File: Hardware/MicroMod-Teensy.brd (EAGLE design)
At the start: 22 x 22.8 mm, 82 parts, among them J1 MICROMOD-2222, Q1 20V/4.2A/52mΩ/1.4W, Q2 20V/0.2A/8MHz/1.2Ω/1Vth, U1 IMXRT1062DV10X10, U3 MKL02Z32VFG4, U4 W25QXX128MBIT-6X5, Y1 32.768kHz, Y2 24MHz

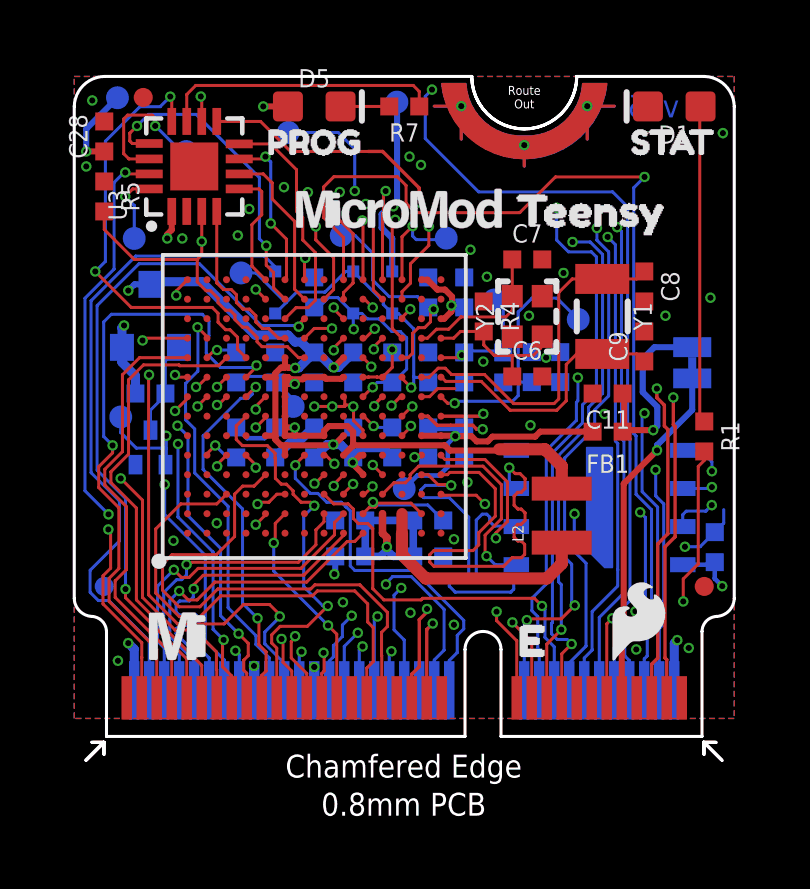
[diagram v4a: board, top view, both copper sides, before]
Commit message: Adding production panel files
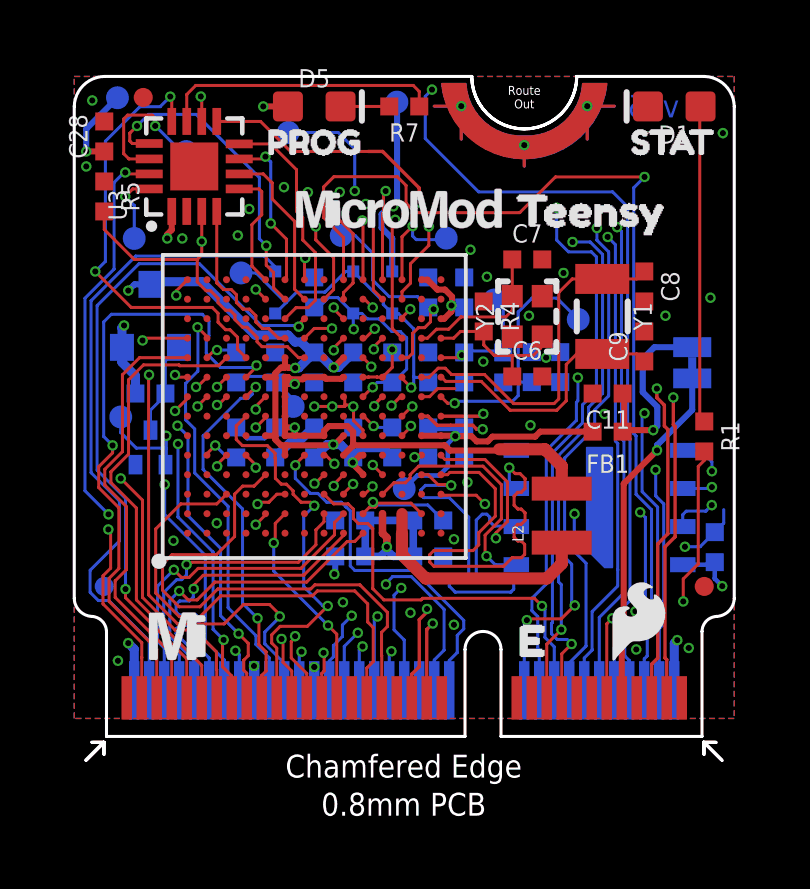
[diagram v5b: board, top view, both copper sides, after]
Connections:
- net SWD_CLK: no longer J1.21
- net SWD_DIO: no longer J1.23
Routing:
- net SWD_DIO: track 36.2 -> 2.43 mm, vias 3 -> 1
- net SWD_CLK: track 37.0 -> 4.89 mm, vias 3 -> 1
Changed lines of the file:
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@@
 <?xml version="1.0" encoding="utf-8"?>
 <!DOCTYPE eagle SYSTEM "eagle.dtd">
-<eagle version="9.6.0">
+<eagle version="9.5.2">
 <drawing>
 <settings>
@@
 <setting verticaltext="up"/>
 </settings>
-<grid distance="1" unitdist="mm" unit="mm" style="lines" multiple="1" display="yes" altdistance="0.1" altunitdist="mm" altunit="mm"/>
+<grid distance="0.05" unitdist="inch" unit="inch" style="lines" multiple="1" display="yes" altdistance="0.005" altunitdist="inch" altunit="inch"/>
 <layers>
-<layer number="1" name="Top" color="4" fill="1" visible="yes" active="yes"/>
-<layer number="2" name="Vert-GND" color="1" fill="3" visible="no" active="yes"/>
+<layer number="1" name="Top" color="4" fill="1" visible="no" active="yes"/>
+<layer number="2" name="Vert-GND" color="1" fill="3" visible="yes" active="yes"/>
 <layer number="15" name="Horz-3V3" color="4" fill="6" visible="no" active="yes"/>
-<layer number="16" name="Bottom" color="1" fill="1" visible="yes" active="yes"/>
+<layer number="16" name="Bottom" color="1" fill="1" visible="no" active="yes"/>
 <layer number="17" name="Pads" color="2" fill="1" visible="yes" active="yes"/>
 <layer number="18" name="Vias" color="2" fill="1" visible="yes" active="yes"/>
 <layer number="19" name="Unrouted" color="6" fill="1" visible="yes" active="yes"/>
 <layer number="20" name="Dimension" color="24" fill="1" visible="yes" active="yes"/>
-<layer number="21" name="tPlace" color="16" fill="1" visible="yes" active="yes"/>
-<layer number="22" name="bPlace" color="14" fill="1" visible="yes" active="yes"/>
-<layer number="23" name="tOrigins" color="15" fill="1" visible="yes" active="yes"/>
-<layer number="24" name="bOrigins" color="15" fill="1" visible="yes" active="yes"/>
+<layer number="21" name="tPlace" color="16" fill="1" visible="no" active="yes"/>
+<layer number="22" name="bPlace" color="14" fill="1" visible="no" active="yes"/>
+<layer number="23" name="tOrigins" color="15" fill="1" visible="no" active="yes"/>
+<layer number="24" name="bOrigins" color="15" fill="1" visible="no" active="yes"/>
 <layer number="25" name="tNames" color="7" fill="1" visible="no" active="yes"/>
 <layer number="26" name="bNames" color="7" fill="1" visible="no" active="yes"/>
@@
 <layer number="43" name="vRestrict" color="2" fill="10" visible="no" active="yes"/>
 <layer number="44" name="Drills" color="7" fill="1" visible="no" active="yes"/>
-<layer number="45" name="Holes" color="7" fill="1" visible="yes" active="yes"/>
+<layer number="45" name="Holes" color="7" fill="1" visible="no" active="yes"/>
 <layer number="46" name="Milling" color="3" fill="1" visible="no" active="yes"/>
 <layer number="47" name="Measures" color="7" fill="1" visible="no" active="yes"/>
 <layer number="48" name="Document" color="7" fill="1" visible="no" active="yes"/>
-<layer number="49" name="Reference" color="7" fill="1" visible="yes" active="yes"/>
+<layer number="49" name="Reference" color="7" fill="1" visible="no" active="yes"/>
 <layer number="50" name="dxf" color="7" fill="1" visible="no" active="yes"/>
-<layer number="51" name="tDocu" color="6" fill="1" visible="yes" active="yes"/>
+<layer number="51" name="tDocu" color="6" fill="1" visible="no" active="yes"/>
 <layer number="52" name="bDocu" color="7" fill="1" visible="no" active="yes"/>
 <layer number="91" name="Nets" color="2" fill="1" visible="no" active="no"/>
@@
 <wire x1="3.561" y1="19.487" x2="2.7" y2="20.348" width="0.1016" layer="16"/>
 <wire x1="2.7" y1="20.348" x2="2.7" y2="20.34" width="0.1016" layer="16"/>
-<via x="14.605" y="3.7913" extent="1-16" drill="0.2"/>
-<via x="11.176" y="19.31865" extent="1-16" drill="0.2"/>
-<wire x1="14.605" y1="3.7877125" x2="14.605" y2="3.7913" width="0.1016" layer="1"/>
-<wire x1="15.25" y1="3.1427125" x2="14.605" y2="3.7877125" width="0.1016" layer="1"/>
-<wire x1="15.25" y1="1.275" x2="15.25" y2="3.1427125" width="0.1016" layer="1"/>
-<wire x1="11.176" y1="19.31865" x2="10.5141" y2="19.98055" width="0.1016" layer="15"/>
-<wire x1="2.7" y1="20.34" x2="3.05945" y2="19.98055" width="0.1016" layer="15"/>
-<wire x1="10.5141" y1="19.98055" x2="3.05945" y2="19.98055" width="0.1016" layer="15"/>
-<wire x1="14.605" y1="3.7913" x2="14.605" y2="4.05461875" width="0.1143" layer="2"/>
-<wire x1="14.605" y1="4.05461875" x2="17.31485" y2="6.76446875" width="0.1143" layer="2"/>
-<wire x1="13.23074375" y1="19.37495" x2="11.2323" y2="19.37495" width="0.1143" layer="2"/>
-<wire x1="17.31485" y1="15.29084375" x2="13.23074375" y2="19.37495" width="0.1143" layer="2"/>
-<contactref element="J1" pad="21"/>
-<wire x1="11.2323" y1="19.37495" x2="11.176" y2="19.31865" width="0.1143" layer="2"/>
-<wire x1="17.31485" y1="6.76446875" x2="17.319" y2="6.76861875" width="0.1016" layer="2"/>
-<wire x1="17.319" y1="15.28669375" x2="17.31485" y2="15.29084375" width="0.1016" layer="2"/>
-<wire x1="17.319" y1="6.76861875" x2="17.319" y2="15.28669375" width="0.1016" layer="2"/>
 <wire x1="1.6468" y1="19.4162" x2="1.6468" y2="20.5698" width="0.1016" layer="1"/>
 <wire x1="1.6468" y1="20.5698" x2="1.778" y2="20.701" width="0.1016" layer="1"/>
@@
 <wire x1="1.7" y1="17.99" x2="2" y2="17.69" width="0.1016" layer="16"/>
 <wire x1="2" y1="17.69" x2="2" y2="16.59" width="0.1016" layer="16"/>
-<via x="14.078" y="4.15" extent="1-16" drill="0.2"/>
-<via x="11.557" y="19.04" extent="1-16" drill="0.2"/>
-<wire x1="14.75" y1="3.178" x2="14.078" y2="3.85" width="0.1016" layer="1"/>
-<wire x1="14.078" y1="3.85" x2="14.078" y2="4.15" width="0.1016" layer="1"/>
-<wire x1="14.75" y1="3.178" x2="14.75" y2="1.275" width="0.1016" layer="1"/>
-<wire x1="14.078" y1="4.15" x2="14.39505" y2="4.15" width="0.1143" layer="2"/>
-<wire x1="14.39505" y1="4.15" x2="17.09895" y2="6.8539" width="0.1143" layer="2"/>
-<wire x1="17.09895" y1="15.13305" x2="13.192" y2="19.04" width="0.1143" layer="2"/>
-<wire x1="13.192" y1="19.04" x2="11.557" y2="19.04" width="0.1143" layer="2"/>
-<contactref element="J1" pad="23"/>
-<wire x1="17.09895" y1="6.8539" x2="17.1158" y2="6.87075" width="0.1016" layer="2"/>
-<wire x1="17.1158" y1="15.1162" x2="17.09895" y2="15.13305" width="0.1016" layer="2"/>
-<wire x1="17.1158" y1="6.87075" x2="17.1158" y2="15.1162" width="0.1016" layer="2"/>
-<wire x1="11.557" y1="19.04" x2="11.3620625" y2="19.04" width="0.1016" layer="15"/>
-<wire x1="11.3620625" y1="19.04" x2="11.3121125" y2="18.99005" width="0.1016" layer="15"/>
-<wire x1="11.3121125" y1="18.99005" x2="11.0398875" y2="18.99005" width="0.1016" layer="15"/>
-<wire x1="11.0398875" y1="18.99005" x2="10.8474" y2="19.1825375" width="0.1016" layer="15"/>
-<wire x1="10.8474" y1="19.1825375" x2="10.8474" y2="19.35988125" width="0.1016" layer="15"/>
-<wire x1="10.8474" y1="19.35988125" x2="10.42993125" y2="19.77735" width="0.1016" layer="15"/>
-<wire x1="10.42993125" y1="19.77735" x2="3.48735" y2="19.77735" width="0.1016" layer="15"/>
-<wire x1="3.48735" y1="19.77735" x2="1.7" y2="17.99" width="0.1016" layer="15"/>
 </signal>
 <signal name="USB_D-" class="1">

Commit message: Move trace away from top edge
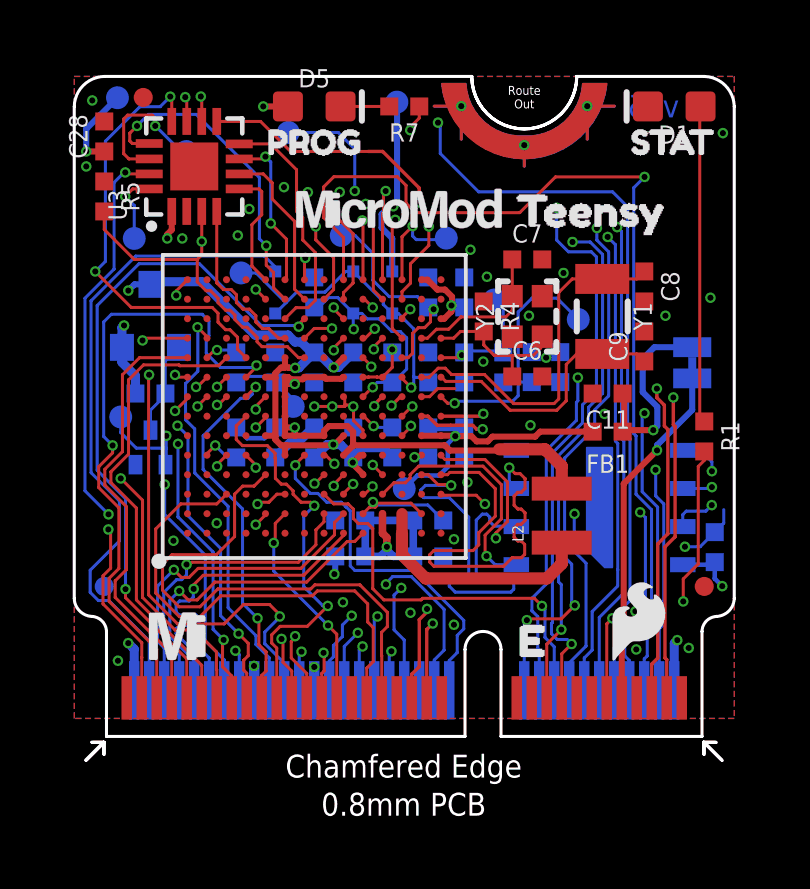
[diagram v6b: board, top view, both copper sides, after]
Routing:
- net PROGRAM: track 34.8 -> 33.9 mm
- net N$12: track 9.36 -> 9.70 mm, vias 0 -> 2
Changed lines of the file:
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@@
 <setting verticaltext="up"/>
 </settings>
-<grid distance="0.05" unitdist="inch" unit="inch" style="lines" multiple="1" display="yes" altdistance="0.005" altunitdist="inch" altunit="inch"/>
+<grid distance="1" unitdist="mm" unit="mm" style="lines" multiple="1" display="yes" altdistance="0.1" altunitdist="mm" altunit="mm"/>
 <layers>
 <layer number="1" name="Top" color="4" fill="1" visible="no" active="yes"/>
-<layer number="2" name="Vert-GND" color="1" fill="3" visible="yes" active="yes"/>
-<layer number="15" name="Horz-3V3" color="4" fill="6" visible="no" active="yes"/>
+<layer number="2" name="Vert-GND" color="1" fill="3" visible="no" active="yes"/>
+<layer number="15" name="Horz-3V3" color="4" fill="6" visible="yes" active="yes"/>
 <layer number="16" name="Bottom" color="1" fill="1" visible="no" active="yes"/>
 <layer number="17" name="Pads" color="2" fill="1" visible="yes" active="yes"/>
@@
 <wire x1="18.5238" y1="9.92411875" x2="18.4452" y2="10.00271875" width="0.1016" layer="16"/>
 <wire x1="13.48" y1="18.143" x2="17.945" y2="18.143" width="0.1016" layer="16"/>
-<wire x1="4.2188875" y1="21.3211125" x2="11.6961125" y2="21.3211125" width="0.1016" layer="15"/>
-<wire x1="11.6961125" y1="21.3211125" x2="11.925" y2="21.55" width="0.1016" layer="15"/>
-<via x="11.925" y="21.55" extent="1-16" drill="0.2"/>
-<wire x1="11.925" y1="21.55" x2="11.7" y2="21.325" width="0.1016" layer="16"/>
-<wire x1="11.7" y1="21.325" x2="11.7" y2="19.923" width="0.1016" layer="16"/>
-<wire x1="11.7" y1="19.923" x2="13.48" y2="18.143" width="0.1016" layer="16"/>
+<wire x1="4.2188875" y1="21.3211125" x2="11.2538875" y2="21.3211125" width="0.1016" layer="15"/>
+<wire x1="11.2538875" y1="21.3211125" x2="12.125" y2="20.45" width="0.1016" layer="15"/>
+<via x="12.125" y="20.45" extent="1-16" drill="0.2"/>
+<wire x1="12.125" y1="20.45" x2="12.2" y2="20.375" width="0.1016" layer="16"/>
+<wire x1="12.2" y1="20.375" x2="12.2" y2="19.423" width="0.1016" layer="16"/>
+<wire x1="12.2" y1="19.423" x2="13.48" y2="18.143" width="0.1016" layer="16"/>
 </signal>
 <signal name="VDD_USB_CAP">
@@
 <contactref element="U3" pad="11"/>
 <contactref element="R7" pad="1"/>
-<wire x1="3.75" y1="20.49" x2="3.75" y2="21.39" width="0.1016" layer="1"/>
-<wire x1="3.75" y1="21.39" x2="4.05" y2="21.69" width="0.1016" layer="1"/>
-<wire x1="11.3" y1="21.69" x2="11.5" y2="21.49" width="0.1016" layer="1"/>
-<wire x1="11.5" y1="21.49" x2="11.5" y2="20.99" width="0.1016" layer="1"/>
-<wire x1="4.05" y1="21.69" x2="11.3" y2="21.69" width="0.1016" layer="1"/>
+<wire x1="3.75" y1="20.49" x2="3.75" y2="21.25" width="0.1016" layer="1"/>
+<wire x1="3.75" y1="21.25" x2="3.7" y2="21.3" width="0.1016" layer="1"/>
+<via x="3.7" y="21.3" extent="1-16" drill="0.2"/>
+<via x="11.2" y="20.2" extent="1-16" drill="0.2"/>
+<wire x1="3.7" y1="21.3" x2="3.7752875" y2="21.3" width="0.1016" layer="15"/>
+<wire x1="10.7386" y1="20.6614" x2="11.2" y2="20.2" width="0.1016" layer="15"/>
+<wire x1="3.7752875" y1="21.3" x2="4.4138875" y2="20.6614" width="0.1016" layer="15"/>
+<wire x1="4.4138875" y1="20.6614" x2="10.7386" y2="20.6614" width="0.1016" layer="15"/>
+<wire x1="11.5" y1="20.6" x2="11.2" y2="20.3" width="0.1016" layer="1"/>
+<wire x1="11.2" y1="20.2" x2="11.2" y2="20.3" width="0.1016" layer="1"/>
+<wire x1="11.5" y1="20.6" x2="11.5" y2="20.99" width="0.1016" layer="1"/>
 </signal>
 <signal name="N$13">
@@
 <via x="21.6206" y="20.1" extent="1-16" drill="0.2"/>
 <wire x1="6.3" y1="20.99" x2="11.0093625" y2="20.99" width="0.1524" layer="15"/>
-<wire x1="12.354" y1="20.946" x2="14.1" y2="19.2" width="0.1524" layer="15"/>
+<wire x1="11.054" y1="20.946" x2="12.8" y2="19.2" width="0.1524" layer="15"/>
 <wire x1="11.0093625" y1="20.99" x2="11.0533625" y2="20.946" width="0.1524" layer="15"/>
-<wire x1="11.0533625" y1="20.946" x2="12.354" y2="20.946" width="0.1524" layer="15"/>
-<wire x1="14.1" y1="19.2" x2="20.7206" y2="19.2" width="0.1524" layer="15"/>
+<wire x1="11.0533625" y1="20.946" x2="11.054" y2="20.946" width="0.1524" layer="15"/>
+<wire x1="12.8" y1="19.2" x2="20.7206" y2="19.2" width="0.1524" layer="15"/>
 <wire x1="20.7206" y1="19.2" x2="21.6206" y2="20.1" width="0.1524" layer="15"/>
 <contactref element="FB2" pad="1"/>

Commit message: Move trace away from edge to pass DFM requirements
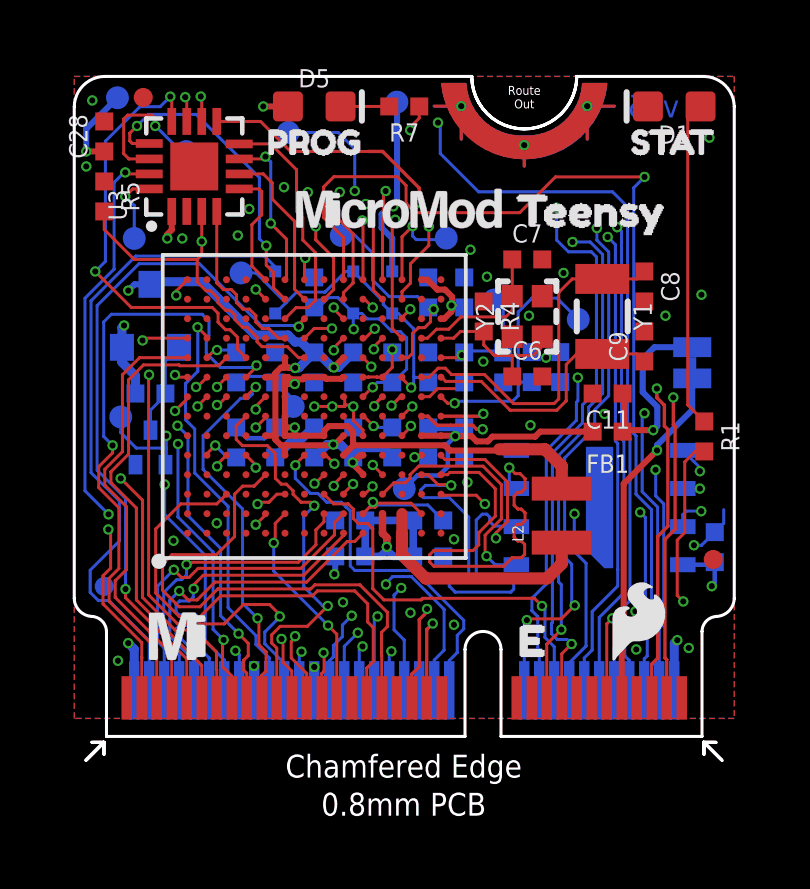
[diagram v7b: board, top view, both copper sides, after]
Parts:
- moved FD1 0.95 mm to (21.3, 5.89)
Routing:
- net QSPI0: track 14.5 -> 13.6 mm
- net QSPI3: track 14.5 -> 13.7 mm
- net 3.3V_CONTROLLED: track 86.3 -> 85.5 mm
- net QSPI-CLK: track 14.5 -> 13.9 mm
